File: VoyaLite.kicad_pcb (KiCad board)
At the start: 2 copper layers, 142.7 x 142.6 mm, 125 parts

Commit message: change things
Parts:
- removed the D1 at (45.2, 122.1)
- removed the D10 at (83.2, 117.1)
- removed the D11 at (83.2, 98.1)
- removed the D12 at (83.2, 79.1)
- removed the D13 at (83.2, 60.1)
- removed the D14 at (83.2, 41.1)
- removed the D15 at (102.2, 112.1)
- removed the D16 at (102.2, 93.1)
- removed the D17 at (102.2, 74.1)
- removed the D18 at (102.2, 55.1)
- removed the D19 at (102.2, 36.1)
- removed the D2 at (45.2, 103.1)
- removed the D20 at (121.2, 117.1)
- removed the D21 at (121.2, 98.1)
- removed the D22 at (121.2, 79.1)
- removed the D23 at (121.2, 60.1)
- removed the D24 at (121.2, 41.1)
- removed the D25 at (140.2, 122.1)
- removed the D26 at (140.2, 103.1)
- removed the D27 at (140.2, 84.1)
- removed the D28 at (140.2, 65.1)
- removed the D29 at (140.2, 46.1)
- removed the D3 at (45.2, 84.1)
- removed the D30 at (146.9, 148.6)
- removed the D31 at (163.4, 158.1)
- removed the D32 at (31.7, 122.1)
- removed the D33 at (31.7, 103.1)
- removed the D34 at (31.7, 84.1)
- removed the D35 at (31.7, 65.1)
- removed the D36 at (50.7, 122.1)
- removed the D37 at (50.7, 103.1)
- removed the D38 at (50.7, 84.1)
- removed the D39 at (50.7, 65.1)
- removed the D4 at (45.2, 65.1)
- removed the D40 at (50.7, 46.1)
- removed the D41 at (69.7, 117.1)
- removed the D42 at (69.7, 98.1)
- removed the D43 at (69.7, 79.1)
- removed the D44 at (69.7, 60.1)
- removed the D45 at (69.7, 41.1)
- removed the D46 at (88.7, 112.1)
- removed the D47 at (88.7, 93.1)
- removed the D48 at (88.7, 74.1)
- removed the D49 at (88.7, 55.1)
- removed the D5 at (64.2, 122.1)
- removed the D50 at (88.7, 36.1)
- removed the D51 at (107.7, 117.1)
- removed the D52 at (107.7, 98.1)
- removed the D53 at (107.7, 79.1)
- removed the D54 at (107.7, 60.1)
- removed the D55 at (107.7, 41.1)
- removed the D56 at (126.7, 122.1)
- removed the D57 at (126.7, 103.1)
- removed the D58 at (126.7, 84.1)
- removed the D59 at (126.7, 65.1)
- removed the D6 at (64.2, 103.1)
- removed the D60 at (126.7, 46.1)
- removed the D61 at (135.2, 141.8)
- removed the D62 at (151.7, 151.3)
- removed the D7 at (64.2, 84.1)
- removed the D8 at (64.2, 65.1)
- removed the D9 at (64.2, 46.1)
- removed the LED1 at (57.4, 53.4)
- removed the LED10 at (57.4, 72.4)
- removed the LED11 at (38.4, 72.4)
- removed the LED12 at (38.4, 91.4)
- removed the LED13 at (57.4, 91.4)
- removed the LED14 at (76.4, 86.4)
- removed the LED15 at (95.4, 81.4)
- removed the LED16 at (114.4, 86.4)
- removed the LED17 at (133.4, 91.4)
- removed the LED18 at (133.4, 110.4)
- removed the LED19 at (114.4, 105.4)
- removed the LED2 at (76.4, 48.4)
- removed the LED20 at (95.4, 100.4)
- removed the LED21 at (76.4, 105.4)
- removed the LED22 at (57.4, 110.4)
- removed the LED23 at (38.4, 110.4)
- removed the LED25 at (57.4, 129.4)
- removed the LED26 at (76.4, 124.4)
- removed the LED27 at (95.4, 119.4)
- removed the LED28 at (114.4, 124.4)
- removed the LED29 at (133.4, 129.4)
- removed the LED3 at (95.4, 43.4)
- removed the LED30 at (137.4, 151.6)
- removed the LED31 at (153.8, 161.1)
- removed the LED4 at (114.4, 48.4)
- removed the LED5 at (133.4, 53.4)
- removed the LED6 at (133.4, 72.4)
- removed the LED7 at (114.4, 67.4)
- removed the LED8 at (95.4, 62.4)
- removed the LED9 at (76.4, 67.4)
- removed the S10 at (76.4, 118.1)
- removed the S11 at (76.4, 99.1)
- removed the S12 at (76.4, 80.1)
- removed the S13 at (76.4, 61.1)
- removed the S14 at (76.4, 42.1)
- removed the S15 at (95.4, 113.1)
- removed the S16 at (95.4, 94.1)
- removed the S17 at (95.4, 75.1)
- removed the S18 at (95.4, 56.1)
- removed the S19 at (95.4, 37.1)
- removed the S2 at (38.4, 104.1)
- removed the S20 at (114.4, 118.1)
- removed the S21 at (114.4, 99.1)
- removed the S22 at (114.4, 80.1)
- removed the S23 at (114.4, 61.1)
- removed the S24 at (114.4, 42.1)
- removed the S25 at (133.4, 123.1)
- removed the S26 at (133.4, 104.1)
- removed the S27 at (133.4, 85.1)
- removed the S28 at (133.4, 66.1)
- removed the S29 at (133.4, 47.1)
- removed the S3 at (38.4, 85.1)
- removed the S30 at (140.6, 146.1)
- removed the S31 at (157.0, 155.6)
- removed the S4 at (38.4, 66.1)
- removed the S5 at (57.4, 123.1)
- removed the S6 at (57.4, 104.1)
- removed the S7 at (57.4, 85.1)
- removed the S8 at (57.4, 66.1)
- removed the S9 at (57.4, 47.1)
- added C1: C_Small, Capacitor_SMD:C_0805_2012Metric_Pad1.18x1.45mm_HandSolder, F.Cu at (-39.9, 105.3)
- added C10: C_Small, Capacitor_SMD:C_0805_2012Metric_Pad1.18x1.45mm_HandSolder, F.Cu at (-35.1, 105.3)
- added C11: C_Small, Capacitor_SMD:C_0805_2012Metric_Pad1.18x1.45mm_HandSolder, F.Cu at (-35.1, 108.3)
- added C12: C_Small, Capacitor_SMD:C_0805_2012Metric_Pad1.18x1.45mm_HandSolder, F.Cu at (-35.1, 111.3)
- added C13: C_Small, Capacitor_SMD:C_0805_2012Metric_Pad1.18x1.45mm_HandSolder, F.Cu at (-35.1, 114.3)
- added C14: C_Small, Capacitor_SMD:C_0805_2012Metric_Pad1.18x1.45mm_HandSolder, F.Cu at (-35.1, 117.3)
- added C15: C_Small, Capacitor_SMD:C_0805_2012Metric_Pad1.18x1.45mm_HandSolder, F.Cu at (-35.1, 120.3)
- added C16: C_Small, Capacitor_SMD:C_0805_2012Metric_Pad1.18x1.45mm_HandSolder, F.Cu at (-35.1, 123.3)
- added C17: C_Small, Capacitor_SMD:C_0805_2012Metric_Pad1.18x1.45mm_HandSolder, F.Cu at (-35.1, 126.3)
- added C18: C_Small, Capacitor_SMD:C_0805_2012Metric_Pad1.18x1.45mm_HandSolder, F.Cu at (-35.1, 129.4)
- added C19: C_Small, Capacitor_SMD:C_0805_2012Metric_Pad1.18x1.45mm_HandSolder, F.Cu at (-30.3, 105.3)
- added C2: C_Small, Capacitor_SMD:C_0805_2012Metric_Pad1.18x1.45mm_HandSolder, F.Cu at (-39.9, 108.3)
- added C20: C_Small, Capacitor_SMD:C_0805_2012Metric_Pad1.18x1.45mm_HandSolder, F.Cu at (-30.3, 108.3)
- added C21: C_Small, Capacitor_SMD:C_0805_2012Metric_Pad1.18x1.45mm_HandSolder, F.Cu at (-30.3, 111.3)
- added C22: C_Small, Capacitor_SMD:C_0805_2012Metric_Pad1.18x1.45mm_HandSolder, F.Cu at (-30.3, 114.3)
- added C23: C_Small, Capacitor_SMD:C_0805_2012Metric_Pad1.18x1.45mm_HandSolder, F.Cu at (-30.3, 117.3)
- added C24: C_Small, Capacitor_SMD:C_0805_2012Metric_Pad1.18x1.45mm_HandSolder, F.Cu at (-30.3, 120.3)
- added C25: C_Small, Capacitor_SMD:C_0805_2012Metric_Pad1.18x1.45mm_HandSolder, F.Cu at (-30.3, 123.3)
- added C26: C_Small, Capacitor_SMD:C_0805_2012Metric_Pad1.18x1.45mm_HandSolder, F.Cu at (-30.3, 126.3)
- added C27: C_Small, Capacitor_SMD:C_0805_2012Metric_Pad1.18x1.45mm_HandSolder, F.Cu at (-30.3, 129.4)
- added C28: C_Small, Capacitor_SMD:C_0805_2012Metric_Pad1.18x1.45mm_HandSolder, F.Cu at (-25.5, 105.3)
- added C29: C_Small, Capacitor_SMD:C_0805_2012Metric_Pad1.18x1.45mm_HandSolder, F.Cu at (-25.5, 108.3)
- added C3: C_Small, Capacitor_SMD:C_0805_2012Metric_Pad1.18x1.45mm_HandSolder, F.Cu at (-39.9, 111.3)
- added C30: C_Small, Capacitor_SMD:C_0805_2012Metric_Pad1.18x1.45mm_HandSolder, F.Cu at (-25.5, 111.3)
- added C31: C_Small, Capacitor_SMD:C_0805_2012Metric_Pad1.18x1.45mm_HandSolder, F.Cu at (-25.5, 114.3)
- added C32: 10u, Capacitor_SMD:C_0805_2012Metric_Pad1.18x1.45mm_HandSolder, F.Cu at (-25.5, 117.3)
- added C33: 100n, Capacitor_SMD:C_0805_2012Metric_Pad1.18x1.45mm_HandSolder, F.Cu at (-25.5, 120.3)
- added C34: 10u, Capacitor_SMD:C_0805_2012Metric_Pad1.18x1.45mm_HandSolder, F.Cu at (-25.5, 123.3)
- added C35: 22uF, Capacitor_SMD:C_0805_2012Metric_Pad1.18x1.45mm_HandSolder, F.Cu at (-25.5, 126.3)
- added C4: C_Small, Capacitor_SMD:C_0805_2012Metric_Pad1.18x1.45mm_HandSolder, F.Cu at (-39.9, 114.3)
- added C40: 100n, Capacitor_SMD:C_0805_2012Metric_Pad1.18x1.45mm_HandSolder, F.Cu at (-25.5, 129.4)
- added C5: C_Small, Capacitor_SMD:C_0805_2012Metric_Pad1.18x1.45mm_HandSolder, F.Cu at (-39.9, 117.3)
- added C6: C_Small, Capacitor_SMD:C_0805_2012Metric_Pad1.18x1.45mm_HandSolder, F.Cu at (-39.9, 120.3)
- added C7: C_Small, Capacitor_SMD:C_0805_2012Metric_Pad1.18x1.45mm_HandSolder, F.Cu at (-39.9, 123.3)
- added C8: C_Small, Capacitor_SMD:C_0805_2012Metric_Pad1.18x1.45mm_HandSolder, F.Cu at (-39.9, 126.3)
- added C9: C_Small, Capacitor_SMD:C_0805_2012Metric_Pad1.18x1.45mm_HandSolder, F.Cu at (-39.9, 129.4)
- added D1: D, Diode_SMD:D_MiniMELF, F.Cu at (-61.4, 36.4)
- added D1: , ceoloide:diode_tht_sod123, B.Cu at (72.0, 125.8)
- added D10: D, Diode_SMD:D_MiniMELF, F.Cu at (-55.0, 36.4)
- added D10: , ceoloide:diode_tht_sod123, B.Cu at (109.0, 120.8)
- added D11: D, Diode_SMD:D_MiniMELF, F.Cu at (-55.0, 39.7)
- added D11: , ceoloide:diode_tht_sod123, B.Cu at (109.0, 102.3)
- added D12: D, Diode_SMD:D_MiniMELF, F.Cu at (-55.0, 43.1)
- added D12: , ceoloide:diode_tht_sod123, B.Cu at (109.0, 83.8)
- added D13: D, Diode_SMD:D_MiniMELF, F.Cu at (-55.0, 46.4)
- added D13: , ceoloide:diode_tht_sod123, B.Cu at (109.0, 65.3)
- added D14: D, Diode_SMD:D_MiniMELF, F.Cu at (-55.0, 49.7)
- added D14: , ceoloide:diode_tht_sod123, B.Cu at (109.0, 46.8)
- added D15: D, Diode_SMD:D_MiniMELF, F.Cu at (-55.0, 53.1)
- added D15: , ceoloide:diode_tht_sod123, B.Cu at (127.5, 115.8)
- added D16: D, Diode_SMD:D_MiniMELF, F.Cu at (-55.0, 56.4)
- added D16: , ceoloide:diode_tht_sod123, B.Cu at (127.5, 97.3)
- added D17: D, Diode_SMD:D_MiniMELF, F.Cu at (-55.0, 59.8)
- added D17: , ceoloide:diode_tht_sod123, B.Cu at (127.5, 78.8)
- added D18: D, Diode_SMD:D_MiniMELF, F.Cu at (-55.0, 63.1)
- added D18: , ceoloide:diode_tht_sod123, B.Cu at (127.5, 60.3)
- added D19: D, Diode_SMD:D_MiniMELF, F.Cu at (-48.6, 36.4)
- added D19: , ceoloide:diode_tht_sod123, B.Cu at (127.5, 41.8)
- added D2: D, Diode_SMD:D_MiniMELF, F.Cu at (-61.4, 39.7)
- added D2: , ceoloide:diode_tht_sod123, B.Cu at (72.0, 107.3)
- added D20: D, Diode_SMD:D_MiniMELF, F.Cu at (-48.6, 39.7)
- added D20: , ceoloide:diode_tht_sod123, B.Cu at (146.0, 120.8)
- added D21: D, Diode_SMD:D_MiniMELF, F.Cu at (-48.6, 43.1)
- added D21: , ceoloide:diode_tht_sod123, B.Cu at (146.0, 102.3)
- added D22: D, Diode_SMD:D_MiniMELF, F.Cu at (-48.6, 46.4)
- added D22: , ceoloide:diode_tht_sod123, B.Cu at (146.0, 83.8)
- added D23: D, Diode_SMD:D_MiniMELF, F.Cu at (-48.6, 49.7)
- added D23: , ceoloide:diode_tht_sod123, B.Cu at (146.0, 65.3)
- added D24: D, Diode_SMD:D_MiniMELF, F.Cu at (-48.6, 53.1)
- added D24: , ceoloide:diode_tht_sod123, B.Cu at (146.0, 46.8)
- added D25: D, Diode_SMD:D_MiniMELF, F.Cu at (-48.6, 56.4)
- added D25: , ceoloide:diode_tht_sod123, B.Cu at (164.5, 125.8)
- added D26: D, Diode_SMD:D_MiniMELF, F.Cu at (-48.6, 59.8)
- added D26: , ceoloide:diode_tht_sod123, B.Cu at (164.5, 107.3)
- added D27: D, Diode_SMD:D_MiniMELF, F.Cu at (-48.6, 63.1)
- added D27: , ceoloide:diode_tht_sod123, B.Cu at (164.5, 88.8)
- added D28: D, Diode_SMD:D_MiniMELF, F.Cu at (-42.2, 36.4)
- added D28: , ceoloide:diode_tht_sod123, B.Cu at (164.5, 70.3)
- added D29: D, Diode_SMD:D_MiniMELF, F.Cu at (-42.2, 39.7)
- added D29: , ceoloide:diode_tht_sod123, B.Cu at (164.5, 51.8)
- added D3: D, Diode_SMD:D_MiniMELF, F.Cu at (-61.4, 43.1)
- added D3: , ceoloide:diode_tht_sod123, B.Cu at (72.0, 88.8)
- added D30: D, Diode_SMD:D_MiniMELF, F.Cu at (-42.2, 43.1)
- added D30: , ceoloide:diode_tht_sod123, B.Cu at (171.0, 151.9)
- added D31: D, Diode_SMD:D_MiniMELF, F.Cu at (-42.2, 46.4)
- added D31: , ceoloide:diode_tht_sod123, B.Cu at (187.0, 161.1)
- added D32: , ceoloide:diode_tht_sod123, F.Cu at (58.5, 125.8)
- added D32: D, Diode_SMD:D_MiniMELF, F.Cu at (-42.2, 49.7)
- added D33: D, Diode_SMD:D_MiniMELF, F.Cu at (-42.2, 53.1)
- added D33: , ceoloide:diode_tht_sod123, F.Cu at (58.5, 107.3)
- added D34: D, Diode_SMD:D_MiniMELF, F.Cu at (-42.2, 56.4)
- added D34: , ceoloide:diode_tht_sod123, F.Cu at (58.5, 88.8)
- added D35: D, Diode_SMD:D_MiniMELF, F.Cu at (-42.2, 59.8)
- added D35: , ceoloide:diode_tht_sod123, F.Cu at (58.5, 70.3)
- added D36: D, Diode_SMD:D_MiniMELF, F.Cu at (-42.2, 63.1)
- added D36: , ceoloide:diode_tht_sod123, F.Cu at (77.0, 125.8)
- added D37: , ceoloide:diode_tht_sod123, F.Cu at (77.0, 107.3)
- added D37: D, Diode_SMD:D_MiniMELF, F.Cu at (-35.8, 36.4)
- added D38: , ceoloide:diode_tht_sod123, F.Cu at (77.0, 88.8)
- added D38: D, Diode_SMD:D_MiniMELF, F.Cu at (-35.8, 39.7)
- added D39: , ceoloide:diode_tht_sod123, F.Cu at (77.0, 70.3)
- added D39: D, Diode_SMD:D_MiniMELF, F.Cu at (-35.8, 43.1)
- added D4: D, Diode_SMD:D_MiniMELF, F.Cu at (-61.4, 46.4)
- added D4: , ceoloide:diode_tht_sod123, B.Cu at (72.0, 70.3)
- added D40: , ceoloide:diode_tht_sod123, F.Cu at (77.0, 51.8)
- added D40: D, Diode_SMD:D_MiniMELF, F.Cu at (-35.8, 46.4)
- added D41: , ceoloide:diode_tht_sod123, F.Cu at (95.5, 120.8)
- added D41: D, Diode_SMD:D_MiniMELF, F.Cu at (-35.8, 49.7)
- added D42: D, Diode_SMD:D_MiniMELF, F.Cu at (-35.8, 53.1)
- added D42: , ceoloide:diode_tht_sod123, F.Cu at (95.5, 102.3)
- added D43: , ceoloide:diode_tht_sod123, F.Cu at (95.5, 83.8)
- added D43: D, Diode_SMD:D_MiniMELF, F.Cu at (-35.8, 56.4)
- added D44: , ceoloide:diode_tht_sod123, F.Cu at (95.5, 65.3)
- added D44: D, Diode_SMD:D_MiniMELF, F.Cu at (-35.8, 59.8)
- added D45: , ceoloide:diode_tht_sod123, F.Cu at (95.5, 46.8)
- added D45: D, Diode_SMD:D_MiniMELF, F.Cu at (-35.8, 63.1)
- added D46: D, Diode_SMD:D_MiniMELF, F.Cu at (-29.4, 36.4)
- added D46: , ceoloide:diode_tht_sod123, F.Cu at (114.0, 115.8)
- added D47: D, Diode_SMD:D_MiniMELF, F.Cu at (-29.4, 39.7)
- added D47: , ceoloide:diode_tht_sod123, F.Cu at (114.0, 97.3)
- added D48: D, Diode_SMD:D_MiniMELF, F.Cu at (-29.4, 43.1)
- added D48: , ceoloide:diode_tht_sod123, F.Cu at (114.0, 78.8)
- added D49: D, Diode_SMD:D_MiniMELF, F.Cu at (-29.4, 46.4)
- added D49: , ceoloide:diode_tht_sod123, F.Cu at (114.0, 60.3)
- added D5: D, Diode_SMD:D_MiniMELF, F.Cu at (-61.4, 49.7)
- added D5: , ceoloide:diode_tht_sod123, B.Cu at (90.5, 125.8)
- added D50: , ceoloide:diode_tht_sod123, F.Cu at (114.0, 41.8)
- added D50: D, Diode_SMD:D_MiniMELF, F.Cu at (-29.4, 49.7)
- added D51: D, Diode_SMD:D_MiniMELF, F.Cu at (-29.4, 53.1)
- added D51: , ceoloide:diode_tht_sod123, F.Cu at (132.5, 120.8)
- added D52: , ceoloide:diode_tht_sod123, F.Cu at (132.5, 102.3)
- added D52: D, Diode_SMD:D_MiniMELF, F.Cu at (-29.4, 56.4)
- added D53: D, Diode_SMD:D_MiniMELF, F.Cu at (-29.4, 59.8)
- added D53: , ceoloide:diode_tht_sod123, F.Cu at (132.5, 83.8)
- added D54: , ceoloide:diode_tht_sod123, F.Cu at (132.5, 65.3)
- added D54: D, Diode_SMD:D_MiniMELF, F.Cu at (-29.4, 63.1)
- added D55: , ceoloide:diode_tht_sod123, F.Cu at (132.5, 46.8)
- added D55: D, Diode_SMD:D_MiniMELF, F.Cu at (-23.0, 36.4)
- added D56: , ceoloide:diode_tht_sod123, F.Cu at (151.0, 125.8)
- added D56: D, Diode_SMD:D_MiniMELF, F.Cu at (-23.0, 39.7)
- added D57: D, Diode_SMD:D_MiniMELF, F.Cu at (-23.0, 43.1)
- added D57: , ceoloide:diode_tht_sod123, F.Cu at (151.0, 107.3)
- added D58: D, Diode_SMD:D_MiniMELF, F.Cu at (-23.0, 46.4)
- added D58: , ceoloide:diode_tht_sod123, F.Cu at (151.0, 88.8)
- added D59: , ceoloide:diode_tht_sod123, F.Cu at (151.0, 70.3)
- added D59: D, Diode_SMD:D_MiniMELF, F.Cu at (-23.0, 49.7)
- added D6: D, Diode_SMD:D_MiniMELF, F.Cu at (-61.4, 53.1)
- added D6: , ceoloide:diode_tht_sod123, B.Cu at (90.5, 107.3)
- added D60: , ceoloide:diode_tht_sod123, F.Cu at (151.0, 51.8)
- added D60: D, Diode_SMD:D_MiniMELF, F.Cu at (-23.0, 53.1)
- added D61: D, Diode_SMD:D_MiniMELF, F.Cu at (-23.0, 56.4)
- added D61: , ceoloide:diode_tht_sod123, F.Cu at (159.3, 145.1)
- added D62: , ceoloide:diode_tht_sod123, F.Cu at (175.4, 154.4)
- added D62: D, Diode_SMD:D_MiniMELF, F.Cu at (-23.0, 59.8)
- added D7: D, Diode_SMD:D_MiniMELF, F.Cu at (-61.4, 56.4)
- added D7: , ceoloide:diode_tht_sod123, B.Cu at (90.5, 88.8)
- added D8: D, Diode_SMD:D_MiniMELF, F.Cu at (-61.4, 59.8)
- added D8: , ceoloide:diode_tht_sod123, B.Cu at (90.5, 70.3)
- added D9: D, Diode_SMD:D_MiniMELF, F.Cu at (-61.4, 63.1)
- added D9: , ceoloide:diode_tht_sod123, B.Cu at (90.5, 51.8)
- added J1: Conn_01x02_Socket, Connector_JST:JST_ZH_B2B-ZR_1x02_P1.50mm_Vertical, F.Cu at (-29.9, 133.2)
- added JP1: SolderJumper_2_Open, Jumper:SolderJumper-2_P1.3mm_Open_RoundedPad1.0x1.5mm, F.Cu at (-62.4, 149.8)
- added L2: 2u2H, Inductor_SMD:L_Vishay_IFSC-1515AH_4x4x1.8mm, F.Cu at (-23.1, 133.6)
- added LED1: SK6812MINI, MX_Alps_Hybrid:SK6803-MINI-E_pia, F.Cu at (65.2, 133.2)
- added LED1: , ceoloide:led_SK6812mini-e (underglow, reversible), B.Cu at (83.7, 59.2)
- added LED10: SK6812MINI, MX_Alps_Hybrid:SK6803-MINI-E_pia, F.Cu at (-52.8, 72.2)
- added LED10: , ceoloide:led_SK6812mini-e (underglow, reversible), B.Cu at (83.7, 77.7)
- added LED11: SK6812MINI, MX_Alps_Hybrid:SK6803-MINI-E_pia, F.Cu at (-52.8, 77.1)
- added LED11: , ceoloide:led_SK6812mini-e (underglow, reversible), B.Cu at (65.2, 77.7)
- added LED12: SK6812MINI, MX_Alps_Hybrid:SK6803-MINI-E_pia, F.Cu at (-52.8, 81.9)
- added LED12: , ceoloide:led_SK6812mini-e (underglow, reversible), B.Cu at (65.2, 96.2)
- added LED13: SK6812MINI, MX_Alps_Hybrid:SK6803-MINI-E_pia, F.Cu at (-52.8, 86.8)
- added LED13: , ceoloide:led_SK6812mini-e (underglow, reversible), B.Cu at (83.7, 96.2)
- added LED14: SK6812MINI, MX_Alps_Hybrid:SK6803-MINI-E_pia, F.Cu at (-52.8, 91.7)
- added LED14: , ceoloide:led_SK6812mini-e (underglow, reversible), B.Cu at (102.2, 91.2)
- added LED15: SK6812MINI, MX_Alps_Hybrid:SK6803-MINI-E_pia, F.Cu at (-52.8, 96.6)
- added LED15: , ceoloide:led_SK6812mini-e (underglow, reversible), B.Cu at (120.7, 86.2)
- added LED16: SK6812MINI, MX_Alps_Hybrid:SK6803-MINI-E_pia, F.Cu at (-52.8, 101.4)
- added LED16: , ceoloide:led_SK6812mini-e (underglow, reversible), B.Cu at (139.2, 91.2)
- added LED17: SK6812MINI, MX_Alps_Hybrid:SK6803-MINI-E_pia, F.Cu at (-44.9, 67.3)
- added LED17: , ceoloide:led_SK6812mini-e (underglow, reversible), B.Cu at (157.7, 96.2)
- added LED18: SK6812MINI, MX_Alps_Hybrid:SK6803-MINI-E_pia, F.Cu at (-44.9, 72.2)
- added LED18: , ceoloide:led_SK6812mini-e (underglow, reversible), B.Cu at (157.7, 114.7)
- added LED19: SK6812MINI, MX_Alps_Hybrid:SK6803-MINI-E_pia, F.Cu at (-44.9, 77.1)
- added LED19: , ceoloide:led_SK6812mini-e (underglow, reversible), B.Cu at (139.2, 109.7)
- added LED2: SK6812MINI, MX_Alps_Hybrid:SK6803-MINI-E_pia, F.Cu at (-60.7, 72.2)
- added LED2: , ceoloide:led_SK6812mini-e (underglow, reversible), B.Cu at (102.2, 54.2)
- added LED20: SK6812MINI, MX_Alps_Hybrid:SK6803-MINI-E_pia, F.Cu at (-44.9, 81.9)
- added LED20: , ceoloide:led_SK6812mini-e (underglow, reversible), B.Cu at (120.7, 104.7)
- added LED21: SK6812MINI, MX_Alps_Hybrid:SK6803-MINI-E_pia, F.Cu at (-44.9, 86.8)
- added LED21: , ceoloide:led_SK6812mini-e (underglow, reversible), B.Cu at (102.2, 109.7)
- added LED22: SK6812MINI, MX_Alps_Hybrid:SK6803-MINI-E_pia, F.Cu at (-44.9, 91.7)
- added LED22: , ceoloide:led_SK6812mini-e (underglow, reversible), B.Cu at (83.7, 114.7)
- added LED23: SK6812MINI, MX_Alps_Hybrid:SK6803-MINI-E_pia, F.Cu at (-44.9, 96.6)
- added LED23: , ceoloide:led_SK6812mini-e (underglow, reversible), B.Cu at (65.2, 114.7)
- added LED25: SK6812MINI, MX_Alps_Hybrid:SK6803-MINI-E_pia, F.Cu at (-37.0, 67.3)
- added LED25: , ceoloide:led_SK6812mini-e (underglow, reversible), B.Cu at (83.7, 133.2)
- added LED26: SK6812MINI, MX_Alps_Hybrid:SK6803-MINI-E_pia, F.Cu at (-37.0, 72.2)
- added LED26: , ceoloide:led_SK6812mini-e (underglow, reversible), B.Cu at (102.2, 128.2)
- added LED27: SK6812MINI, MX_Alps_Hybrid:SK6803-MINI-E_pia, F.Cu at (-37.0, 77.1)
- added LED27: , ceoloide:led_SK6812mini-e (underglow, reversible), B.Cu at (120.7, 123.2)
- added LED28: SK6812MINI, MX_Alps_Hybrid:SK6803-MINI-E_pia, F.Cu at (-37.0, 81.9)
- added LED28: , ceoloide:led_SK6812mini-e (underglow, reversible), B.Cu at (139.2, 128.2)
- added LED29: SK6812MINI, MX_Alps_Hybrid:SK6803-MINI-E_pia, F.Cu at (-37.0, 86.8)
- added LED29: , ceoloide:led_SK6812mini-e (underglow, reversible), B.Cu at (157.7, 133.2)
- added LED3: SK6812MINI, MX_Alps_Hybrid:SK6803-MINI-E_pia, F.Cu at (-60.7, 77.1)
- added LED3: , ceoloide:led_SK6812mini-e (underglow, reversible), B.Cu at (120.7, 49.2)
- added LED30: SK6812MINI, MX_Alps_Hybrid:SK6803-MINI-E_pia, F.Cu at (-37.0, 91.7)
- added LED30: , ceoloide:led_SK6812mini-e (underglow, reversible), B.Cu at (161.5, 154.8)
- added LED31: SK6812MINI, MX_Alps_Hybrid:SK6803-MINI-E_pia, F.Cu at (-37.0, 96.6)
- added LED31: , ceoloide:led_SK6812mini-e (underglow, reversible), B.Cu at (177.5, 164.1)
- added LED4: SK6812MINI, MX_Alps_Hybrid:SK6803-MINI-E_pia, F.Cu at (-60.7, 81.9)
- added LED4: , ceoloide:led_SK6812mini-e (underglow, reversible), B.Cu at (139.2, 54.2)
- added LED5: SK6812MINI, MX_Alps_Hybrid:SK6803-MINI-E_pia, F.Cu at (-60.7, 86.8)
- added LED5: , ceoloide:led_SK6812mini-e (underglow, reversible), B.Cu at (157.7, 59.2)
- added LED6: SK6812MINI, MX_Alps_Hybrid:SK6803-MINI-E_pia, F.Cu at (-60.7, 91.7)
- added LED6: , ceoloide:led_SK6812mini-e (underglow, reversible), B.Cu at (157.7, 77.7)
- added LED7: SK6812MINI, MX_Alps_Hybrid:SK6803-MINI-E_pia, F.Cu at (-60.7, 96.6)
- added LED7: , ceoloide:led_SK6812mini-e (underglow, reversible), B.Cu at (139.2, 72.7)
- added LED8: SK6812MINI, MX_Alps_Hybrid:SK6803-MINI-E_pia, F.Cu at (-60.7, 101.4)
- added LED8: , ceoloide:led_SK6812mini-e (underglow, reversible), B.Cu at (120.7, 67.7)
- added LED9: SK6812MINI, MX_Alps_Hybrid:SK6803-MINI-E_pia, F.Cu at (-52.8, 67.3)
- added LED9: , ceoloide:led_SK6812mini-e (underglow, reversible), B.Cu at (102.2, 72.7)
- added NT1: NetTie_2, NetTie:NetTie-2_THT_Pad0.3mm, F.Cu at (-63.8, 152.3)
- added S10: SW_Push, KeySwitches_DalePrice:Kailh_socket_PG1350_reversible, F.Cu at (-152.0, 92.2)
- added S10: , MX, F.Cu at (102.2, 121.8)
- added S11: , MX, F.Cu at (102.2, 103.3)
- added S11: SW_Push, KeySwitches_DalePrice:Kailh_socket_PG1350_reversible, F.Cu at (-152.0, 142.8)
- added S12: , MX, F.Cu at (102.2, 84.8)
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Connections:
- LED24 pad 1: (no net) -> Net-(LED24-DOUT)
- LED24 pad 2: (no net) -> GND
- LED24 pad 3: (no net) -> Net-(LED23-DOUT)
- LED24 pad 4: (no net) -> +5V
- MCU1 pad 103: (no net) -> GND
- MCU1 pad 104: (no net) -> GND
- MCU1 pad 123: (no net) -> GND
- S1 pad 1: (no net) -> c1
- S1 pad 2: (no net) -> Net-(D1-A)
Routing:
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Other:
- board size 142.7 x 142.6 mm -> 141.3 x 141.6 mm

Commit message: add Traces to pcb
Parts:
- removed C10, C11, C12, C13, C14, C15, C16, C17, C18, C19, C2, C20, C21, C22, C23, C24, C25, C26, C27, C28, C29, C3, C30, C31, C4, C5, C6, C7, C8, C9: C_Small, Capacitor_SMD:C_0805_2012Metric_Pad1.18x1.45mm_HandSolder
- removed C32: 10u, Capacitor_SMD:C_0805_2012Metric_Pad1.18x1.45mm_HandSolder
- removed C33: 100n, Capacitor_SMD:C_0805_2012Metric_Pad1.18x1.45mm_HandSolder
- removed C35: 22uF, Capacitor_SMD:C_0805_2012Metric_Pad1.18x1.45mm_HandSolder
- removed the D1 at (-61.4, 36.4)
- removed the D1 at (72.0, 125.8)
- removed D10, D11, D12, D13, D14, D15, D16, D17, D18, D19, D2, D20, D21, D22, D23, D24, D25, D26, D27, D28, D29, D3, D30, D31, D32, D33, D34, D35, D36, D37, D38, D39, D4, D40, D41, D42, D43, D44, D45, D46, D47, D48, D49, D5, D50, D51, D52, D53, D54, D55, D56, D57, D58, D59, D6, D60, D61, D62, D7, D8, D9: D, Diode_SMD:D_MiniMELF
- removed D10, D11, D12, D13, D14, D15, D16, D17, D18, D19, D2, D20, D21, D22, D23, D24, D25, D26, D27, D28, D29, D3, D30, D31, D32, D33, D34, D35, D36, D37, D38, D39, D4, D40, D41, D42, D43, D44, D45, D46, D47, D48, D49, D5, D50, D51, D52, D53, D54, D55, D56, D57, D58, D59, D6, D60, D61, D62, D7, D8, D9: , ceoloide:diode_tht_sod123
- removed L2: 2u2H, Inductor_SMD:L_Vishay_IFSC-1515AH_4x4x1.8mm
- removed LED1, LED10, LED11, LED12, LED13, LED14, LED15, LED16, LED17, LED18, LED19, LED2, LED20, LED21, LED22, LED23, LED24, LED25, LED26, LED27, LED28, LED29, LED3, LED30, LED31, LED4, LED5, LED6, LED7, LED8, LED9: SK6812MINI, MX_Alps_Hybrid:SK6803-MINI-E_pia
- removed LED1, LED10, LED11, LED12, LED13, LED14, LED15, LED16, LED17, LED18, LED19, LED2, LED20, LED21, LED22, LED23, LED25, LED26, LED27, LED28, LED29, LED3, LED30, LED31, LED4, LED5, LED6, LED7, LED8, LED9: , ceoloide:led_SK6812mini-e (underglow, reversible)
- removed MCU1: , ceoloide:mcu_nice_nano
- removed NT1: NetTie_2, NetTie:NetTie-2_THT_Pad0.3mm
- removed the S10 at (-152.0, 92.2)
- removed the S11 at (-152.0, 142.8)
- removed the S12 at (-131.9, 142.1)
- removed the S13 at (-131.9, 24.8)
- removed the S14 at (-152.0, 75.4)
- removed the S15 at (-152.0, 24.8)
- removed the S16 at (-131.9, 109.1)
- removed the S17 at (-192.3, 125.9)
- removed the S18 at (-172.2, 109.1)
- removed the S19 at (-152.0, 109.1)
- removed the S2 at (-131.9, 92.2)
- removed the S20 at (-192.3, 58.5)
- removed the S21 at (-192.3, 92.2)
- removed the S22 at (-172.2, 24.8)
- removed the S23 at (-172.2, 58.5)
- removed the S24 at (-152.0, 41.7)
- removed the S25 at (-172.2, 142.8)
- removed the S26 at (-192.3, 109.1)
- removed the S27 at (-131.9, 41.7)
- removed the S28 at (-172.2, 41.7)
- removed the S29 at (-172.2, 92.2)
- removed the S3 at (-131.9, 125.9)
- removed the S30 at (-172.2, 75.4)
- removed the S31 at (-192.3, 75.4)
- removed the S4 at (-152.0, 125.9)
- removed the S5 at (-152.0, 58.5)
- removed the S6 at (-172.2, 125.9)
- removed the S7 at (-131.9, 75.4)
- removed the S8 at (-131.9, 58.5)
- removed the S9 at (-192.3, 41.7)
- removed SuperMiniNRF53840: ~, Library_Pia:supermini NRF52840 superflat
- added C36: 1u, Capacitor_SMD:C_0402_1005Metric_Pad0.74x0.62mm_HandSolder, B.Cu at (95.3, 41.4)
- added C37: 4u7, Capacitor_SMD:C_0603_1608Metric_Pad1.08x0.95mm_HandSolder, B.Cu at (86.4, 42.8)
- added C38: 4u7, Capacitor_SMD:C_0603_1608Metric_Pad1.08x0.95mm_HandSolder, B.Cu at (93.5, 44.1)
- added C39: 4u7, Capacitor_SMD:C_0603_1608Metric_Pad1.08x0.95mm_HandSolder, B.Cu at (55.3, 47.8)
- added C41: 10u, Capacitor_SMD:C_0603_1608Metric_Pad1.08x0.95mm_HandSolder, B.Cu at (49.0, 53.6)
- added C42: 10u, Capacitor_SMD:C_0603_1608Metric_Pad1.08x0.95mm_HandSolder, B.Cu at (44.1, 53.6)
- added C43: 100n, Capacitor_SMD:C_0402_1005Metric_Pad0.74x0.62mm_HandSolder, B.Cu at (50.2, 54.2)
- added C44: 100n, Capacitor_SMD:C_0402_1005Metric_Pad0.74x0.62mm_HandSolder, B.Cu at (42.9, 54.2)
- added C45: 100n, Capacitor_SMD:C_0402_1005Metric_Pad0.74x0.62mm_HandSolder, B.Cu at (100.1, 36.0)
- added C46: 100n, Capacitor_SMD:C_0402_1005Metric_Pad0.74x0.62mm_HandSolder, B.Cu at (102.1, 37.8)
- added C47: 7p, Capacitor_SMD:C_0402_1005Metric_Pad0.74x0.62mm_HandSolder, B.Cu at (50.2, 52.0)
- added C48: 10u, Capacitor_SMD:C_0603_1608Metric_Pad1.08x0.95mm_HandSolder, B.Cu at (108.2, 35.8)
- added C49: 7p, Capacitor_SMD:C_0402_1005Metric_Pad0.74x0.62mm_HandSolder, B.Cu at (42.9, 52.0)
- added D1: Orange, Diode_SMD:D_0805_2012Metric_Pad1.15x1.40mm_HandSolder, B.Cu at (84.7, 42.6)
- added J3: USB_C_Receptacle_USB2.0_16P, Library_Pia:USB_C_Receptacle_Bottom_Up SMD, B.Cu at (85.1, 35.3)
- added J4: Conn_01x04_Socket, Connector_PinHeader_2.54mm:PinHeader_1x04_P2.54mm_Vertical, B.Cu at (129.1, 32.5)
- added L1: 10uH, Inductor_SMD:L_APV_ANR5045, B.Cu at (34.3, 60.7)
- added Q1: NTJD1155LT1G, Library_Pia:TRANS_NTJD1155LT1G, B.Cu at (100.0, 37.7)
- added Q2: NTJD1155LT1G, Library_Pia:TRANS_NTJD1155LT1G, B.Cu at (108.1, 38.0)
- added R1: 10K, Capacitor_SMD:C_0402_1005Metric_Pad0.74x0.62mm_HandSolder, B.Cu at (93.7, 42.7)
- added R10: 100K, Capacitor_SMD:C_0402_1005Metric_Pad0.74x0.62mm_HandSolder, B.Cu at (111.4, 37.2)
- added R2: 10K, Capacitor_SMD:C_0402_1005Metric_Pad0.74x0.62mm_HandSolder, B.Cu at (93.7, 40.7)
- added R3: 51K, Capacitor_SMD:C_0402_1005Metric_Pad0.74x0.62mm_HandSolder, B.Cu at (77.7, 38.7)
- added R4: 51K, Capacitor_SMD:C_0402_1005Metric_Pad0.74x0.62mm_HandSolder, B.Cu at (78.7, 38.7)
- added R5: 10K, Capacitor_SMD:C_0402_1005Metric_Pad0.74x0.62mm_HandSolder, B.Cu at (89.0, 45.7)
- added R6: 10K, Capacitor_SMD:C_0402_1005Metric_Pad0.74x0.62mm_HandSolder, B.Cu at (97.0, 37.7)
- added R7: 2K, Capacitor_SMD:C_0402_1005Metric_Pad0.74x0.62mm_HandSolder, B.Cu at (93.7, 41.7)
- added R8: 10K, Capacitor_SMD:C_0402_1005Metric_Pad0.74x0.62mm_HandSolder, B.Cu at (106.0, 38.0)
- added R9: 10K, Capacitor_SMD:C_0402_1005Metric_Pad0.74x0.62mm_HandSolder, B.Cu at (110.4, 37.2)
- added SW2: SW_SPDT_312, Button_Switch_SMD:SW_SPDT_PCM12, B.Cu at (98.3, 32.3)
- added U2: E73-2G4M08S1C, Library_Pia:E73-2G4M08S1C-52840 - reverse, B.Cu at (69.9, 40.4)
- added U4: XC6220B331MR, Package_TO_SOT_SMD:SOT-23-5, B.Cu at (46.5, 53.2)
- added Y1: 32.768kHz, Crystal:Crystal_SMD_HC49-SD_HandSoldering, B.Cu at (64.8, 55.7)
- C1: value C_Small -> 4u7; footprint Capacitor_SMD:C_0805_2012Metric_Pad1.18x1.45mm_HandSolder -> Capacitor_SMD:C_0603_1608Metric_Pad1.08x0.95mm_HandSolder; moved to B.Cu
- C34: value 10u -> 4u7; footprint Capacitor_SMD:C_0805_2012Metric_Pad1.18x1.45mm_HandSolder -> Capacitor_SMD:C_0603_1608Metric_Pad1.08x0.95mm_HandSolder; moved to B.Cu
- C40: footprint Capacitor_SMD:C_0805_2012Metric_Pad1.18x1.45mm_HandSolder -> Capacitor_SMD:C_0402_1005Metric_Pad0.74x0.62mm_HandSolder; moved to B.Cu
- J1, SW1, U3: moved to B.Cu
- JP1: footprint Jumper:SolderJumper-2_P1.3mm_Open_RoundedPad1.0x1.5mm -> Jumper:SolderJumper-2_P1.3mm_Open_TrianglePad1.0x1.5mm; moved to B.Cu
- S1: value SW_Push -> ~; footprint KeySwitches_DalePrice:Kailh_socket_PG1350_reversible -> Library_Pia:Kailh_Low-Profile-Switch_17mm_one Side
- S10, S11, S12, S13, S14, S15, S16, S17, S18, S19, S2, S20, S21, S22, S23, S24, S25, S26, S27, S28, S29, S3, S30, S31, S4, S5, S6, S7, S8, S9: value (none) -> ~; footprint MX -> Library_Pia:Kailh_Low-Profile-Switch_17mm_one Side
- U1: value RP604K501A-TR -> WE-TVS-82400102; footprint Library_Pia:DFN(PL)2730-12 -> Package_TO_SOT_SMD:SOT-23-6; moved to B.Cu
- moved S1 258.1 mm to (65.2, 126.8), turned to 0 degrees
- moved JP1 190.7 mm to (92.7, 38.8)
- moved U3 180.5 mm to (89.6, 42.6), turned to 180 degrees
- moved U1 179.3 mm to (81.9, 42.4), turned to -90 degrees
- moved SW1 176.6 mm to (107.1, 32.3)
- moved J1 176.5 mm to (114.9, 32.1), turned to -90 degrees
- moved C1 134.4 mm to (79.2, 42.8), turned to 90 degrees
- moved C34 122.7 mm to (72.8, 49.8), turned to -90 degrees
- moved C40 115.8 mm to (56.5, 47.6), turned to -90 degrees
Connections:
- C1 pad 1: +5V -> VBUS
- C34 pad 1: LED -> +3V3
- C40 pad 1: Net-(U2A-VDD) -> +3V3
- J1 pad 1: +BATT -> GND
- J1 pad 2: -BATT -> /VBATIn
- JP1 pad 1: LED -> Net-(JP1-A)
- JP1 pad 2: LED_IN -> Net-(JP1-B)
- S10 pad 1: (no net) -> c3
- S10 pad 2: (no net) -> Net-(S10B-A)
- S11 pad 1: (no net) -> c3
- S11 pad 2: (no net) -> Net-(S11B-A)
- S12 pad 1: (no net) -> c3
- S12 pad 2: (no net) -> Net-(S12B-A)
- S13 pad 1: (no net) -> c3
- S13 pad 2: (no net) -> Net-(S13B-A)
- S14 pad 1: (no net) -> c3
- S14 pad 2: (no net) -> Net-(S14B-A)
- S15 pad 1: (no net) -> c4
- S15 pad 2: (no net) -> Net-(S15B-A)
- S16 pad 1: (no net) -> c4
- S16 pad 2: (no net) -> Net-(S16B-A)
- S17 pad 1: (no net) -> c4
- S17 pad 2: (no net) -> Net-(S17B-A)
- S18 pad 1: (no net) -> c4
- S18 pad 2: (no net) -> Net-(S18B-A)
- S19 pad 1: (no net) -> c4
- S19 pad 2: (no net) -> Net-(S19B-A)
- S2 pad 1: (no net) -> c1
- S2 pad 2: (no net) -> Net-(S2B-A)
- S20 pad 1: (no net) -> c5
- S20 pad 2: (no net) -> Net-(S20B-A)
- S21 pad 1: (no net) -> c5
- S21 pad 2: (no net) -> Net-(S21B-A)
- S22 pad 1: (no net) -> c5
- S22 pad 2: (no net) -> Net-(S22B-A)
- S23 pad 1: (no net) -> c5
- S23 pad 2: (no net) -> Net-(S23B-A)
- S24 pad 1: (no net) -> c5
- S24 pad 2: (no net) -> Net-(S24B-A)
- S25 pad 1: (no net) -> c6
- S25 pad 2: (no net) -> Net-(S25B-A)
- S26 pad 1: (no net) -> c6
- S26 pad 2: (no net) -> Net-(S26B-A)
- S27 pad 1: (no net) -> c6
- S27 pad 2: (no net) -> Net-(S27B-A)
- S28 pad 1: (no net) -> c6
- S28 pad 2: (no net) -> Net-(S28B-A)
- S29 pad 1: (no net) -> c6
- S29 pad 2: (no net) -> Net-(S29B-A)
- S3 pad 1: (no net) -> c1
- S3 pad 2: (no net) -> Net-(S3B-A)
- S30 pad 1: (no net) -> c7
- S30 pad 2: (no net) -> Net-(S30B-A)
- S31 pad 1: (no net) -> c7
- S31 pad 2: (no net) -> Net-(S31B-A)
- S4 pad 1: (no net) -> c1
- S4 pad 2: (no net) -> Net-(S4B-A)
- S5 pad 1: (no net) -> c2
- S5 pad 2: (no net) -> Net-(S5B-A)
- S6 pad 1: (no net) -> c2
- S6 pad 2: (no net) -> Net-(S6B-A)
- S7 pad 1: (no net) -> c2
- S7 pad 2: (no net) -> Net-(S7B-A)
- S8 pad 1: (no net) -> c2
- S8 pad 2: (no net) -> Net-(S8B-A)
- S9 pad 1: (no net) -> c2
- S9 pad 2: (no net) -> Net-(S9B-A)
- SW1 pad 1: +3V8 -> /VBATIn
- U1 pad 1: LED -> Net-(J3-D+-PadA6)
- U1 pad 2: Boost_EN -> GND
- U1 pad 3: (no net) -> Net-(J3-D--PadA7)
- U1 pad 4: (no net) -> Net-(U2A-DM)
- U1 pad 5: Net-(U1-AGND) -> VBUS
- U1 pad 6: LED_IN -> Net-(U2A-DP)
- U3 pad 1: unconnected-(U3-TS-Pad1) -> Net-(U3-TS)
- U3 pad 10: +3V8 -> Net-(SW2-A)
- U3 pad 11: +3V8 -> Net-(SW2-A)
- U3 pad 12: Net-(U3-ILIM) -> unconnected-(U3-ILIM-Pad12)
- U3 pad 14: GND -> unconnected-(U3-TMR-Pad14)
- U3 pad 15: unconnected-(U3-SYSOFF-Pad15) -> GND
- U3 pad 16: Net-(U3-ISET) -> Net-(JP1-A)
- U3 pad 17: Net-(U3-VSS-Pad17) -> GND
- U3 pad 2: Bat+ -> +BATT
- U3 pad 3: Bat+ -> +BATT
- U3 pad 5: Bat+ -> GND
- U3 pad 6: GND -> +3V8
- U3 pad 8: Net-(U3-VSS-Pad17) -> GND
- U3 pad 9: unconnected-(U3-~{CHG}-Pad9) -> Net-(D1-K)
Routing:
- net (no net): track 826.7 -> 0.00 mm, vias 90 -> 0
- net r2: track 0.00 -> 275.0 mm
- net r1: track 0.00 -> 223.3 mm
- net r3: track 0.00 -> 184.1 mm
- net r4: track 0.00 -> 138.1 mm
- net VCC: track 0.00 -> 102.6 mm, vias 0 -> 5
- net GND: track 148.9 -> 249.7 mm, vias 31 -> 15
- net r5: track 0.00 -> 95.2 mm
- net Net-(S4C-DOUT): track 0.00 -> 91.6 mm, vias 0 -> 10
- net c2: track 0.00 -> 83.6 mm, vias 0 -> 9
- net VBUS: track 0.00 -> 79.4 mm, vias 0 -> 8
- net c3: track 0.00 -> 74.2 mm, vias 0 -> 8
- net c5: track 0.00 -> 74.1 mm, vias 0 -> 8
- net c4: track 0.00 -> 74.0 mm, vias 0 -> 8
- net c6: track 0.00 -> 74.0 mm, vias 0 -> 8
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- added copper zone on In1.Cu, net +BATT
- added copper zone on In2.Cu, net GND
- added copper zone on In1.Cu, net VBUS
- added copper zone on In1.Cu, net VCC
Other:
- board size 141.3 x 141.6 mm -> 141.4 x 143 mm
- copper layers 2 -> 4

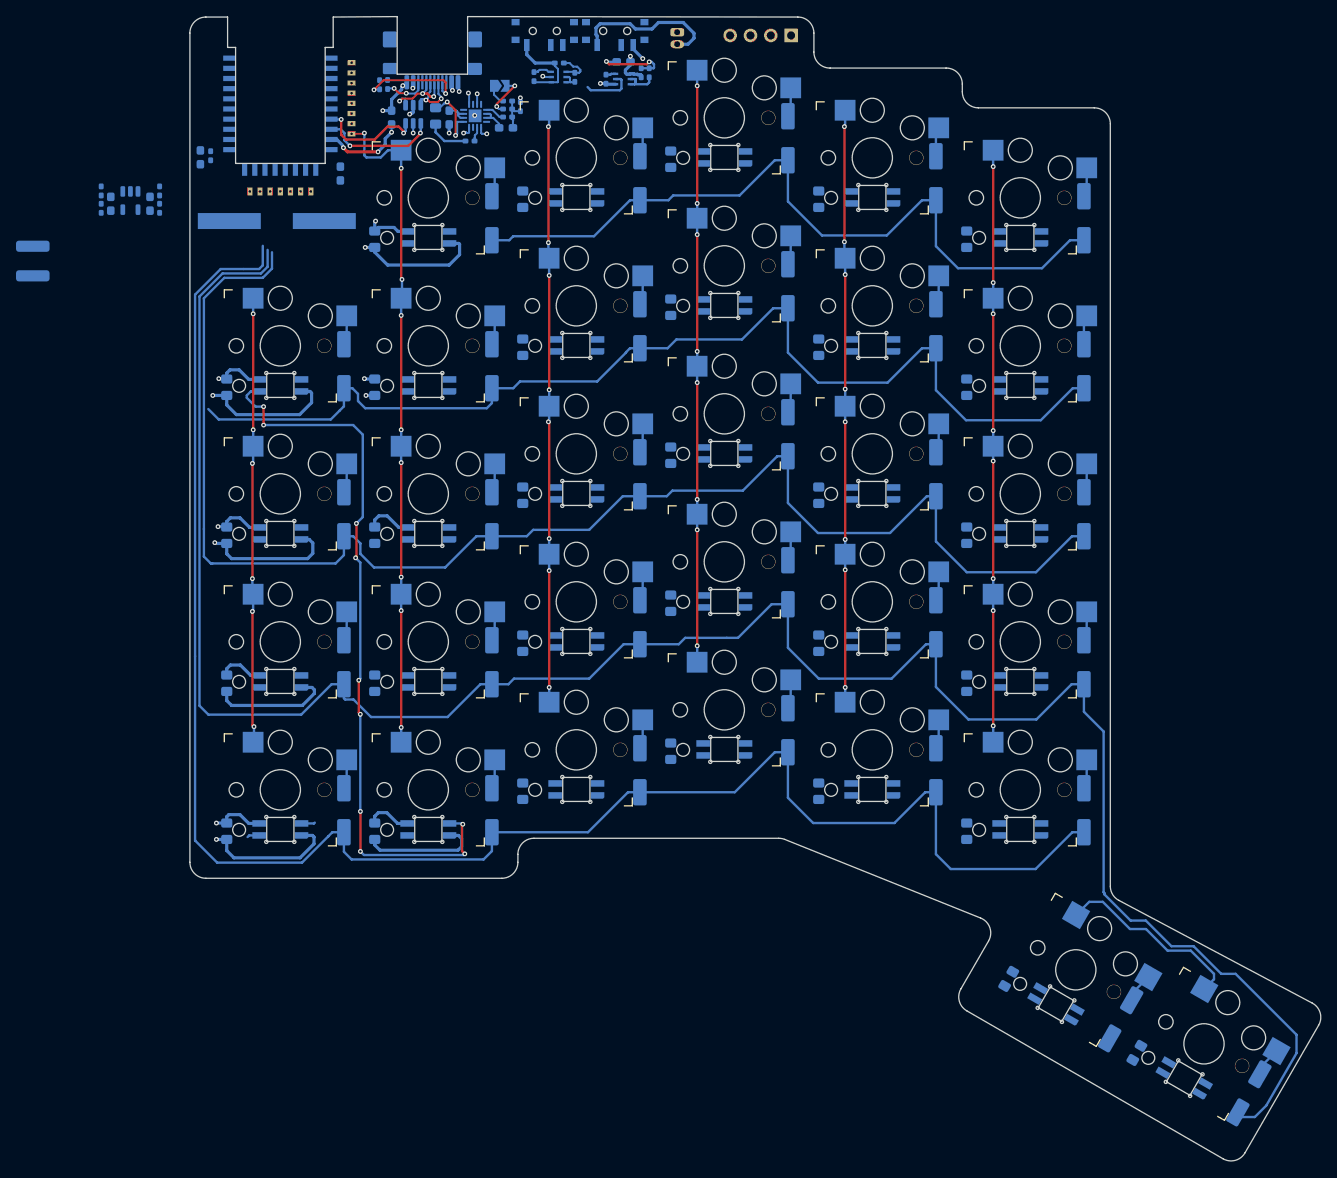
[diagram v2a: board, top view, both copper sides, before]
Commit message: add tracks
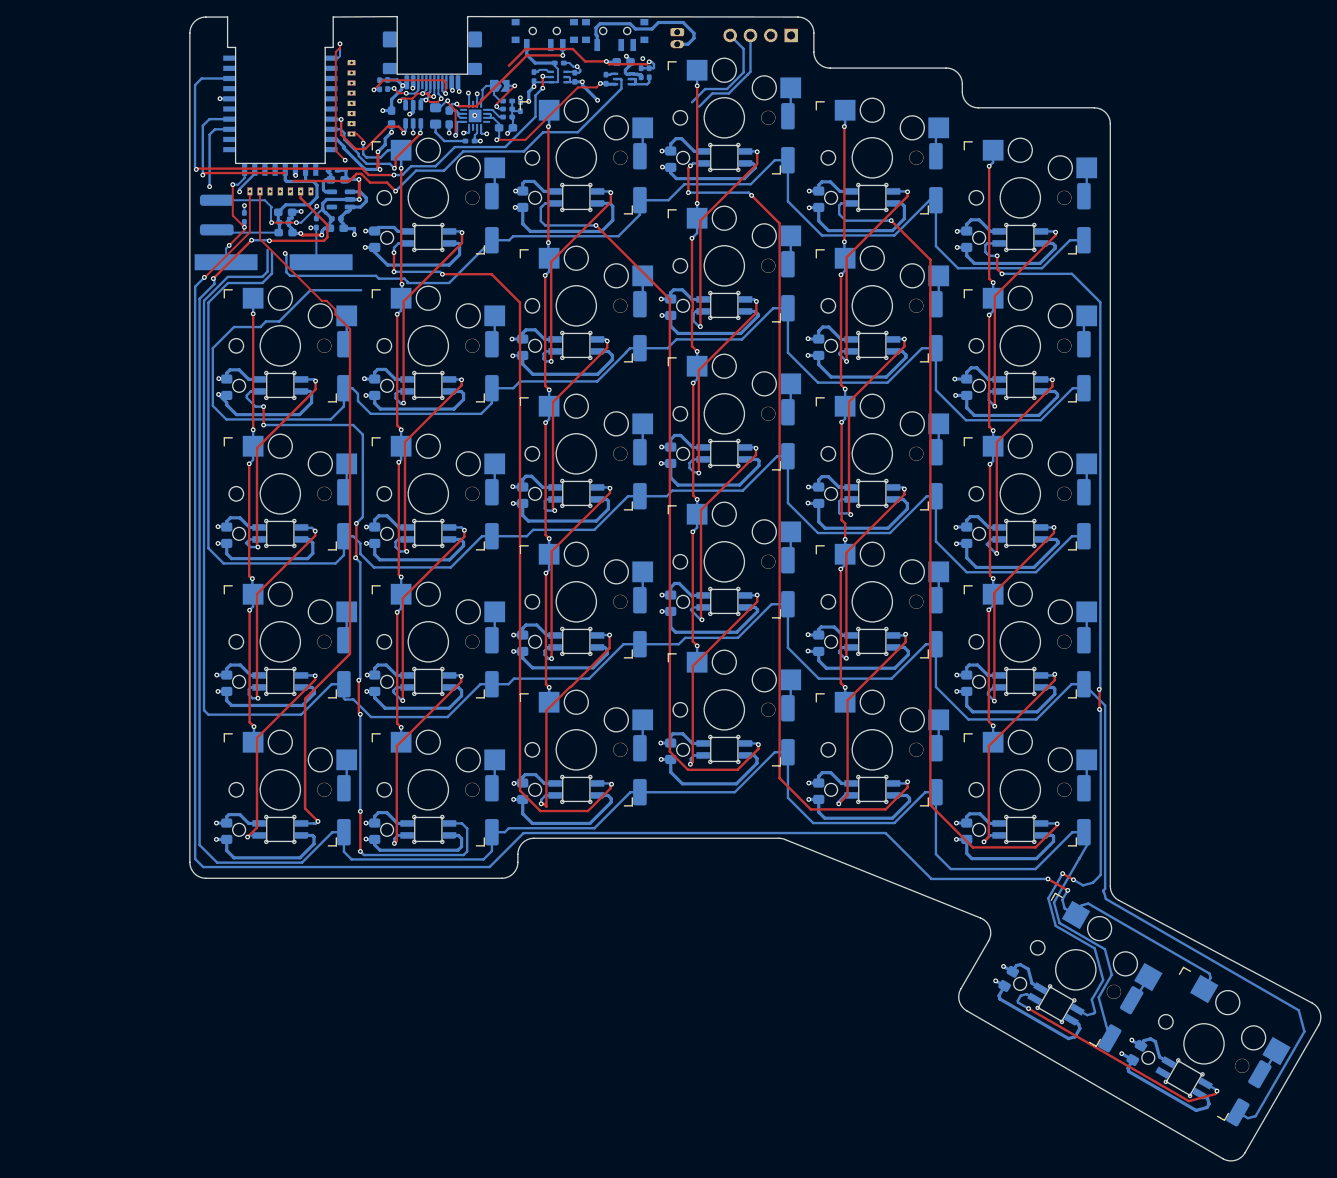
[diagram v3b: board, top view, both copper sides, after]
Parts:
- moved C44 29.4 mm to (71.8, 49.4), turned to 0 degrees
- moved C42 28.5 mm to (72.4, 50.6), turned to 0 degrees
- moved C49 27.2 mm to (69.8, 56.0), turned to 90 degrees
- moved U4 26.3 mm to (72.8, 53.0), turned to 180 degrees
- moved L1 23.7 mm to (57.3, 55.0)
- moved C41 23.5 mm to (72.3, 56.6), turned to 180 degrees
- moved C43 22.1 mm to (72.3, 55.4), turned to 180 degrees
- moved C39 14.2 mm to (65.9, 57.2), turned to 0 degrees
- moved C40 12.4 mm to (65.7, 55.9), turned to 0 degrees
- moved C47 11.1 mm to (60.8, 55.3), turned to 90 degrees
- moved C34 8.43 mm to (65.9, 54.6), turned to 0 degrees
- moved Y1 5.17 mm to (64.4, 60.9)
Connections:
- S13 pad 9: unconnected-(S13-Pad9) -> GND
- SW1 pad 1: /VBATIn -> unconnected-(SW1-B-Pad1)
- SW1 pad 3: +BATT -> unconnected-(SW1-A-Pad3)
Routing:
- net GND: track 249.7 -> 1316.1 mm, vias 15 -> 51
- net VCC: track 102.6 -> 788.0 mm, vias 5 -> 33
- net c7: track 24.1 -> 226.4 mm, vias 0 -> 3
- net Net-(S29C-DOUT): track 0.00 -> 121.7 mm, vias 0 -> 6
- net Net-(S19C-DOUT): track 0.00 -> 108.8 mm, vias 0 -> 4
- net Net-(S24C-DOUT): track 0.00 -> 106.0 mm, vias 0 -> 2
- net Net-(S10C-DIN): track 0.00 -> 99.4 mm, vias 0 -> 4
- net Net-(S14C-DOUT): track 0.00 -> 95.7 mm, vias 0 -> 2
- net LED: track 1.70 -> 88.9 mm, vias 0 -> 1
- net LED_EN: track 1.10 -> 67.6 mm, vias 1 -> 4
- net BAT_MEAS_EN: track 6.35 -> 70.8 mm, vias 0 -> 2
- net r4: track 138.1 -> 185.0 mm, vias 0 -> 2
- net +3V8: track 12.6 -> 59.1 mm, vias 0 -> 4
- net r1: track 223.3 -> 268.2 mm, vias 0 -> 3
- net Net-(S30C-DOUT): track 0.00 -> 33.1 mm, vias 0 -> 2
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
